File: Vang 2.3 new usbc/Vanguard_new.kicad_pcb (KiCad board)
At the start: 4 copper layers, 42.3 x 51.9 mm, 93 parts, among them J1 USB_C_Receptacle_USB2.0_16P, J2 Conn_02x03_Pin, J3 Micro_SD_Card_Det1, J4 STARBOARD_SERVO, J5 PORTSIDE_SERVO, J6 Battery In, J7 EJECTION_SERVO, Q1 BSS138, Q2 BSS138, Q3 BSS138, Q4 BSS138, U1 ATSAMD11D14A-M, U10 BMP390L, U2 ATmega4809-A, U3 AT25DF641A-SH-T, U4 AP2112K-3.3, U5 BD1020HFV, U6 BNO086, U7 TXB0104D, U8 TPS61092, U9 MPM3610AGQV-P, Y1 32.768kHz

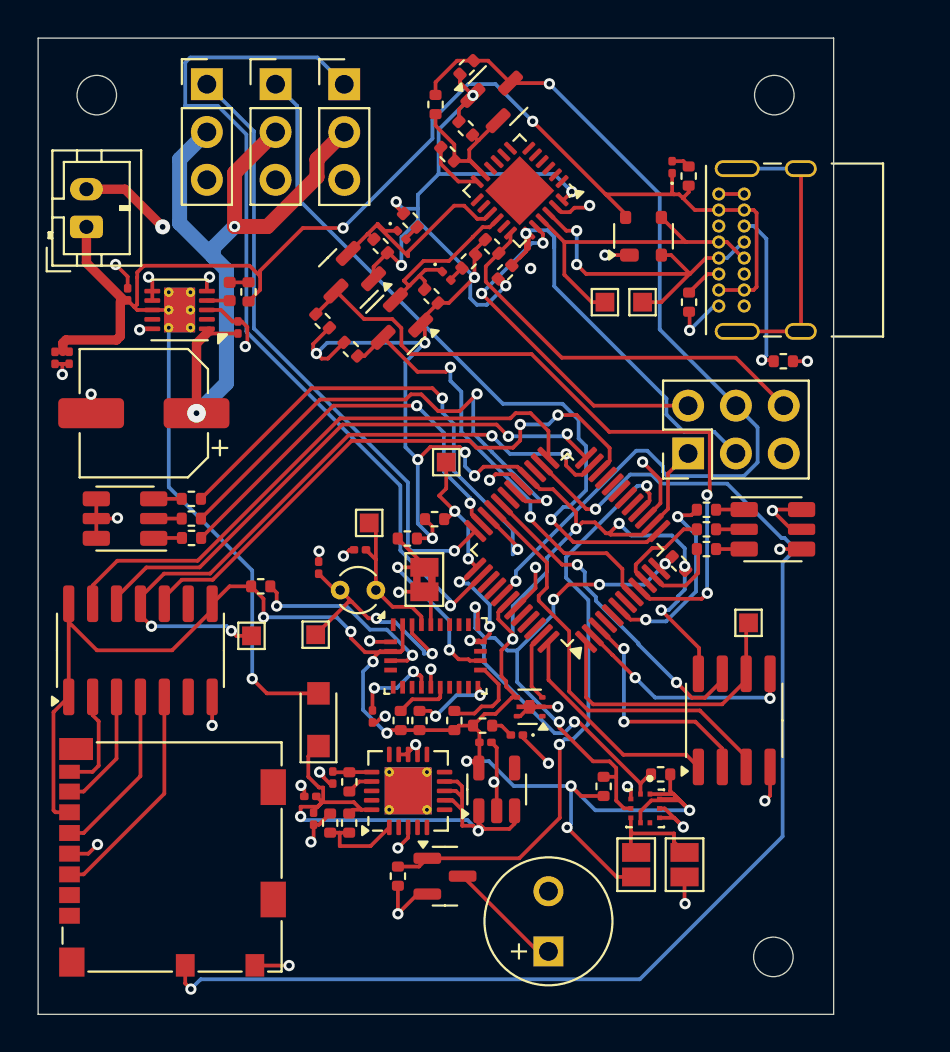
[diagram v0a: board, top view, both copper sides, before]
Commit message: changed footprint
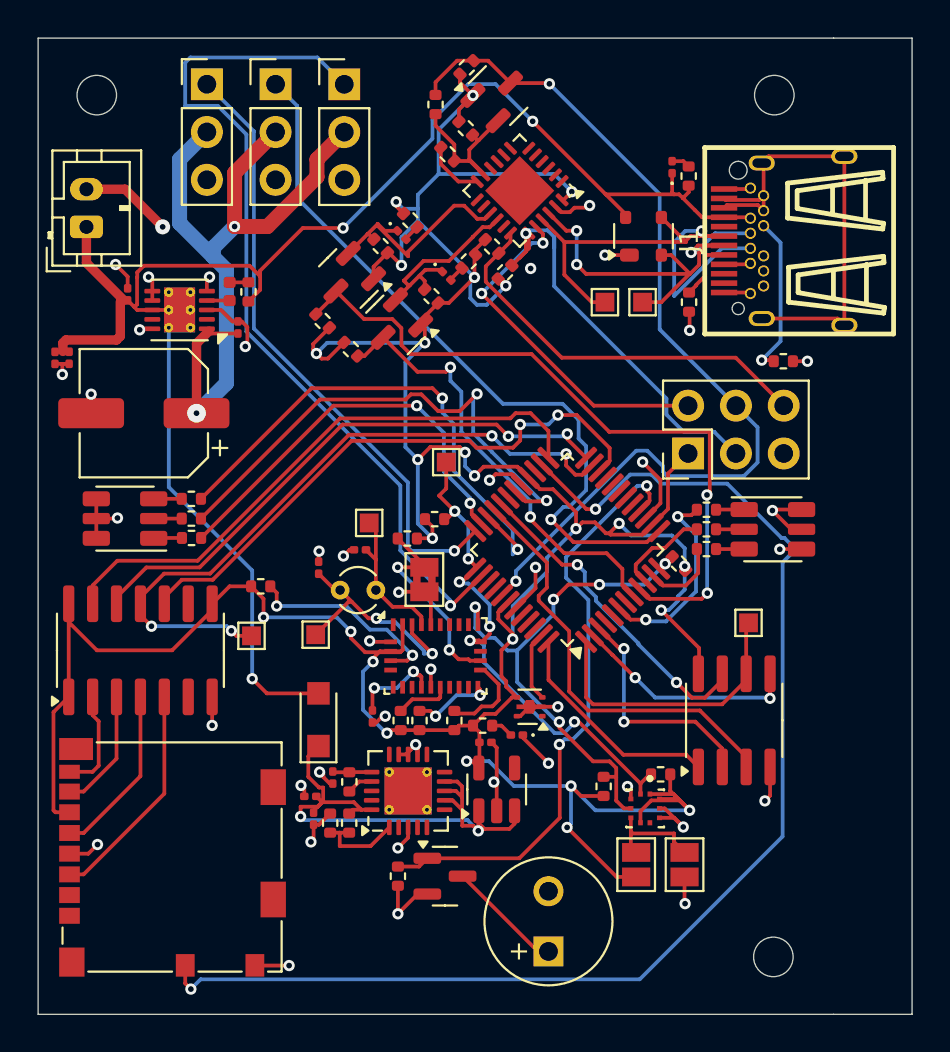
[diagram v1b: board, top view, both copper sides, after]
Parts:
- J1: footprint Connector_USB:USB_C_Receptacle_GCT_USB4085 -> Connector_USB:USB-C-SMD_JLC REPLACEMENT
- moved J1 4.91 mm to (132.0, 94.7)
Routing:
- net (no net): track 0.00 -> 25.1 mm
- net unconnected-(J1-SHIELD-PadS1): track 15.4 -> 0.00 mm
- net Net-(D1-I/O2): track 17.9 -> 27.6 mm, vias 0 -> 1
- net BATT_IN: track 92.7 -> 87.9 mm
- net Net-(D1-I/O1): track 18.5 -> 23.2 mm, vias 2 -> 3
- net Net-(J1-CC1): track 2.00 -> 3.33 mm
- net GND: track 77.9 -> 77.3 mm
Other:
- board size 42.3 x 51.9 mm -> 46.4 x 51.9 mm

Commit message: updated parts
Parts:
- J3: footprint Connector_Card:microSD_HC_Molex_104031-0811 -> Connector_Card:microSD_HC_Hirose_DM3D-SF
- moved J3 1.00 mm to (99.2, 128.5), turned to -90 degrees
- moved C5 0.10 mm to (106.9, 124.2)
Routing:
- net BATT_IN: track 87.9 -> 97.9 mm
- net (no net): track 25.1 -> 29.0 mm
- net Net-(D1-I/O2): track 27.6 -> 24.3 mm
- net +3.3V: track 198.9 -> 201.1 mm, vias 25 -> 27
- net Net-(J3-DAT0): track 6.50 -> 7.81 mm
- net Net-(J3-CLK): track 9.23 -> 10.5 mm
- net Net-(J3-CMD): track 12.0 -> 13.3 mm
- net CD: track 68.4 -> 69.4 mm
- net GND: track 77.3 -> 76.5 mm
- net Net-(J3-DAT1): track 5.47 -> 6.18 mm
- net Net-(J2-Pin_3): track 22.3 -> 21.7 mm
